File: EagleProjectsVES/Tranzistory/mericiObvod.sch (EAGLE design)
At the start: 100 parts, among them IC1 TLC272D, IC2 TLC272D, IC3 NE555D, IC4 NE555D, IC5 TLC271D, K1 M3XXH, K2 M3XXH, K3 M3XXH, K4 M3XXH, T3 BC557B, U12V SMKDSP_1,5/2

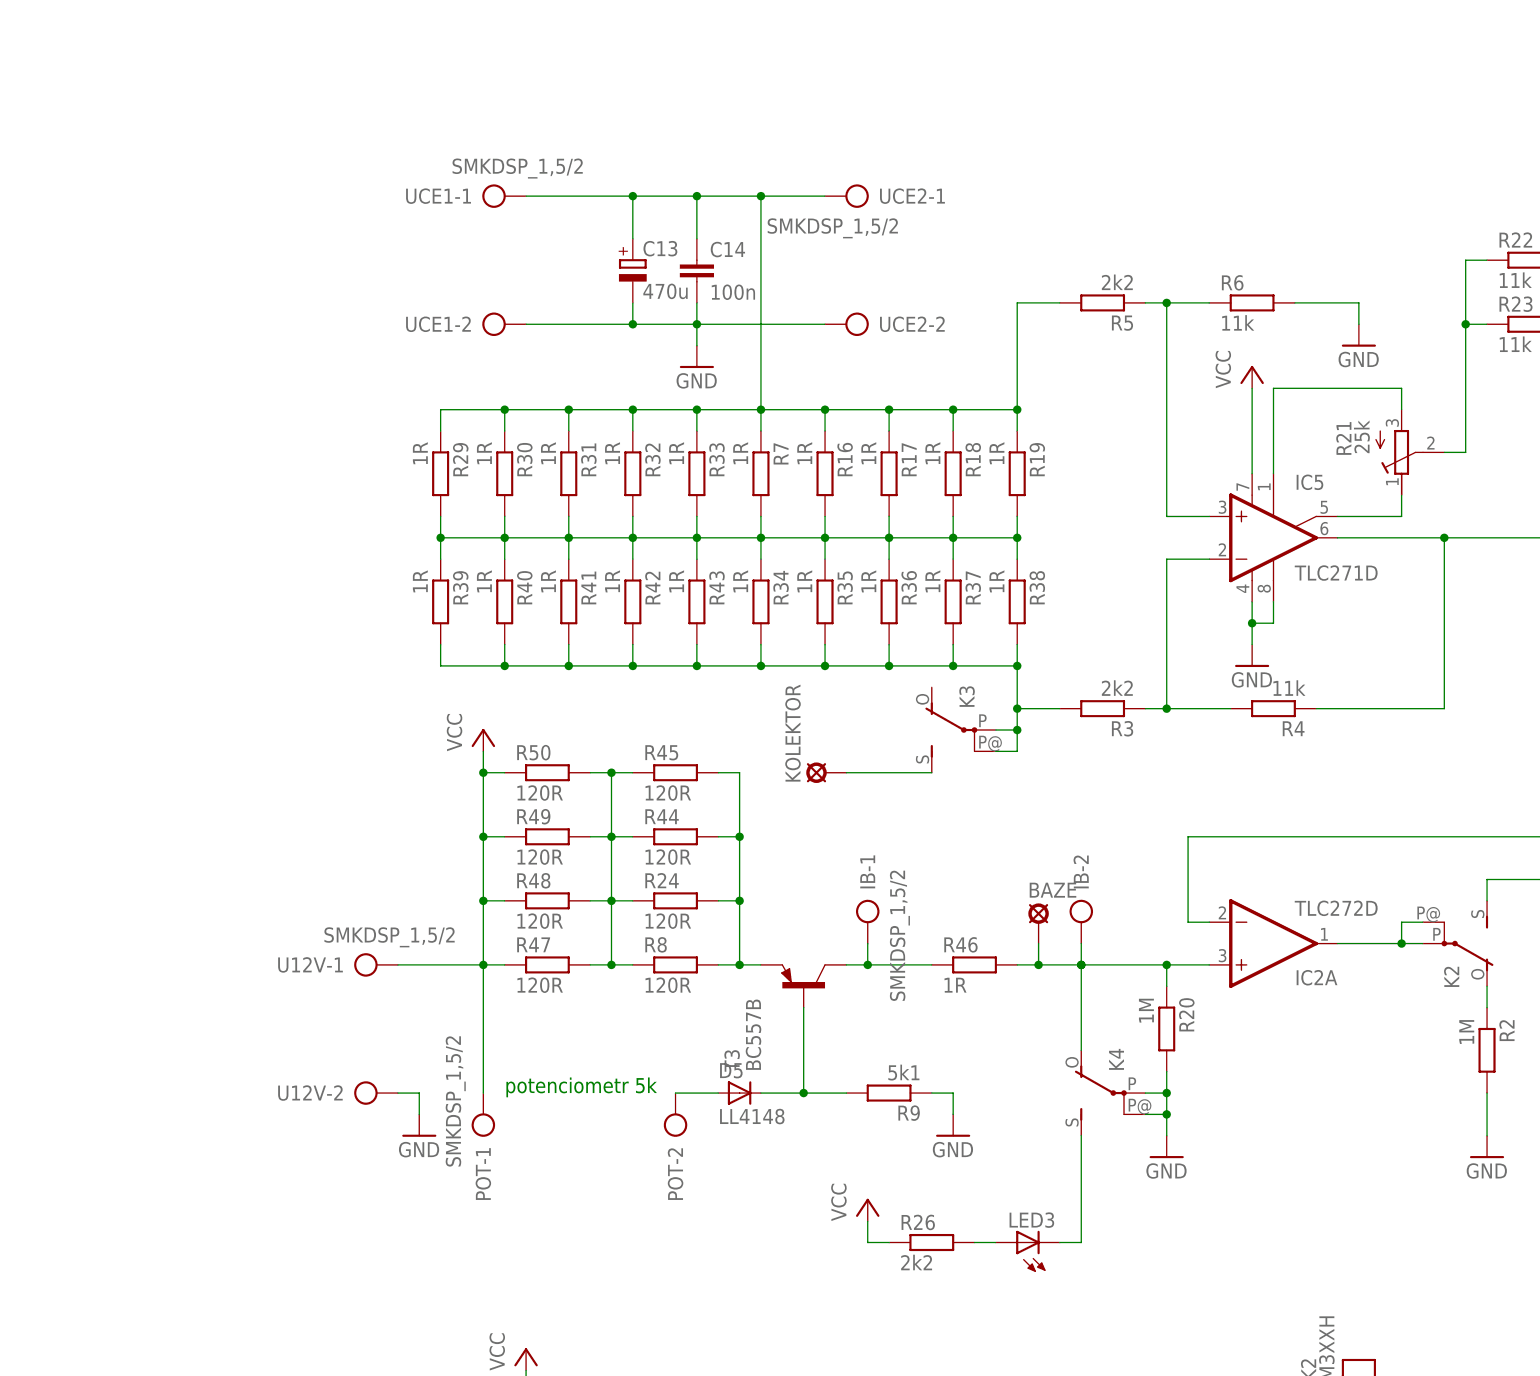
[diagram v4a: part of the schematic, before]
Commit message: DPS Tranzistory: - opraveny chyby v desce, nyni by mela byt pouzitelna az do 30 V UCE
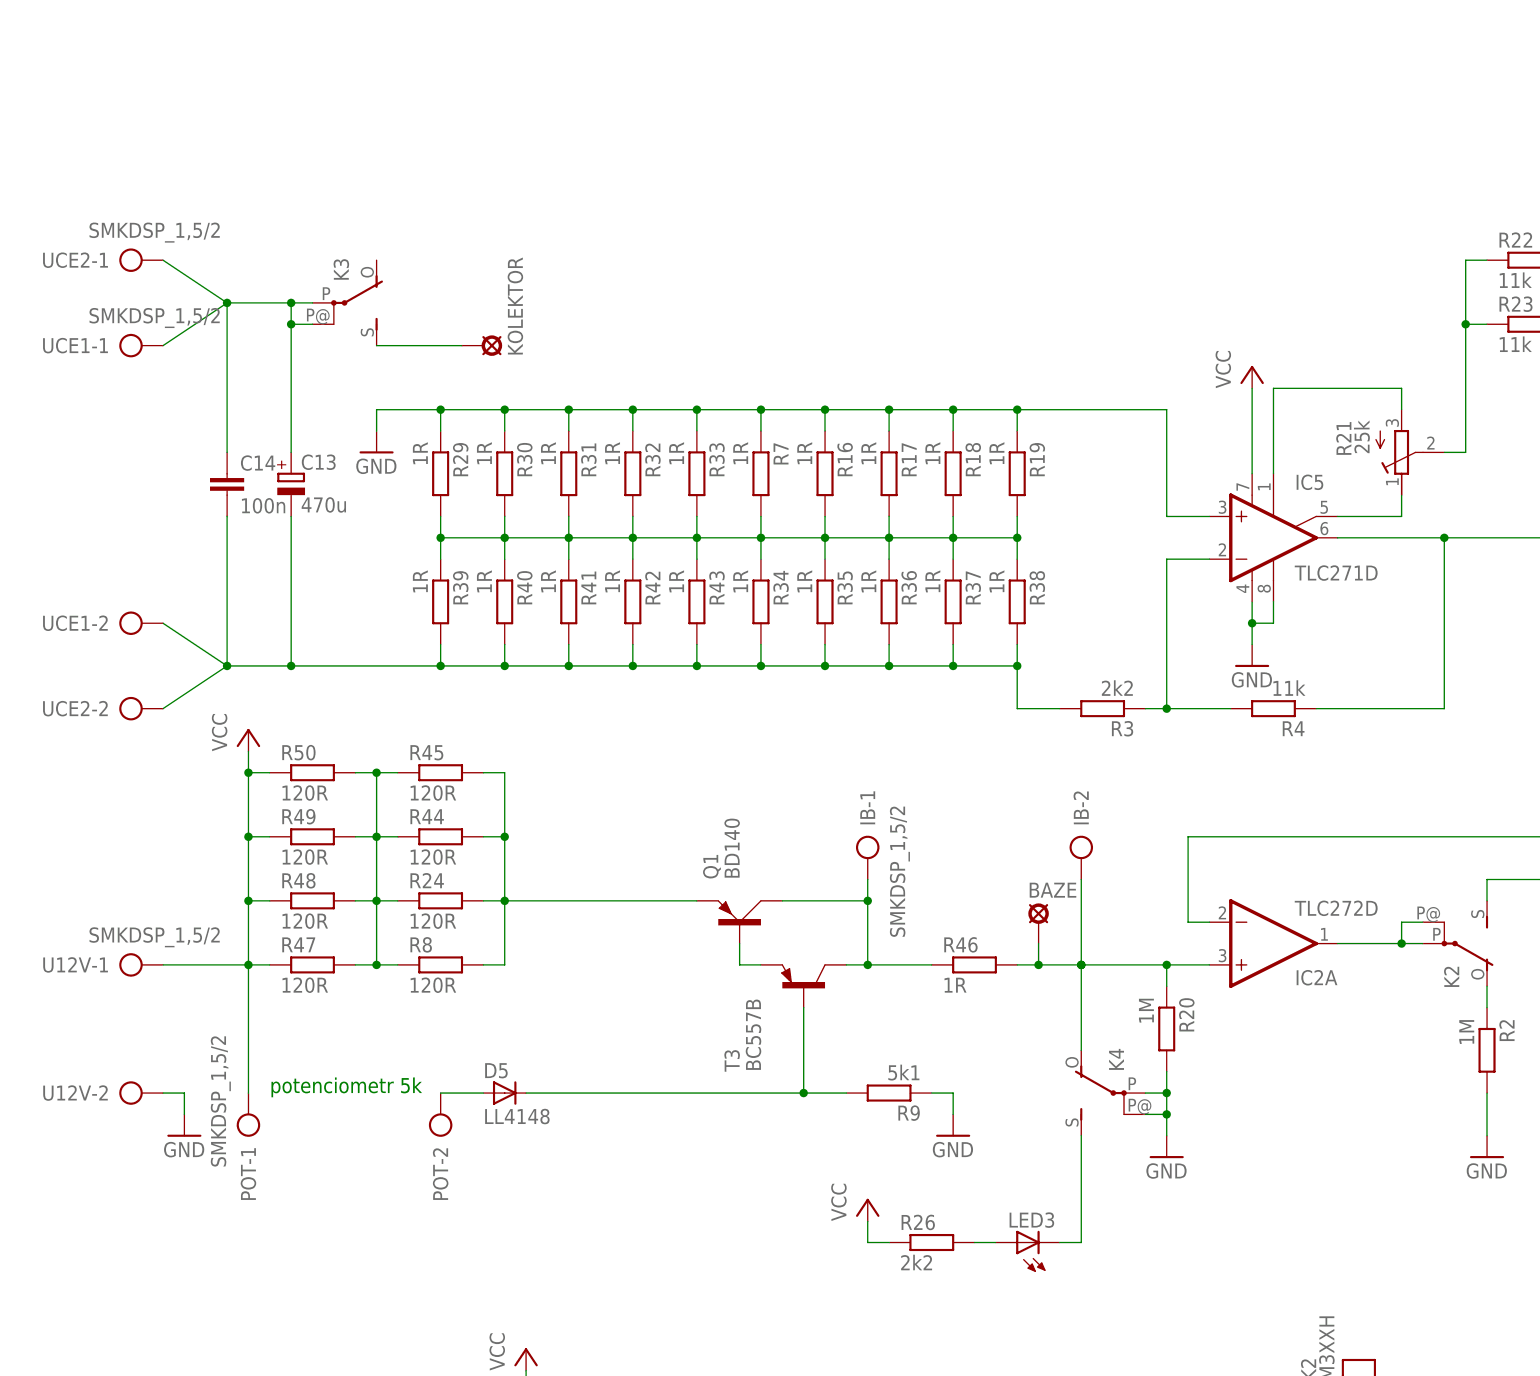
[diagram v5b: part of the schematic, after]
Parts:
- removed R5: 2k2, rcl:R-EU_R0805
- removed R6: 11k, rcl:R-EU_R0805
- added Q1: BD140, transistor-power:BD140
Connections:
- removed net N$11: C13.+, C14.1, R16.1, R17.1, R18.1, R19.1, R29.1, R30.1, R31.1, R32.1, R33.1, R5.2, R7.1, UCE1-1.KL, UCE2-1.KL
- new net N$40: C13.+, C14.1, K32.P, K32.P@1, UCE1-1.KL, UCE2-1.KL
- net GND: now also IC5.+IN, R16.1, R17.1, R18.1, R19.1, R29.1, R30.1, R31.1, R32.1, R33.1, R7.1; no longer C13.-, C14.2, R6.2, UCE1-2.KL, UCE2-2.KL
- net N$16: now also Q1.C
- net N$17: now also Q1.E; no longer T3.E
- net N$48: now also C13.-, C14.2, UCE1-2.KL, UCE2-2.KL; no longer K32.P, K32.P@1
- net N$9: now also Q1.B, T3.E; no longer IC5.+IN, R5.1, R6.1
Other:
- moved on the sheet: C13, C14, D5, IB-1, IB-2, K3, KOLEKTOR, POT-1, POT-2, R24, R44, R45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

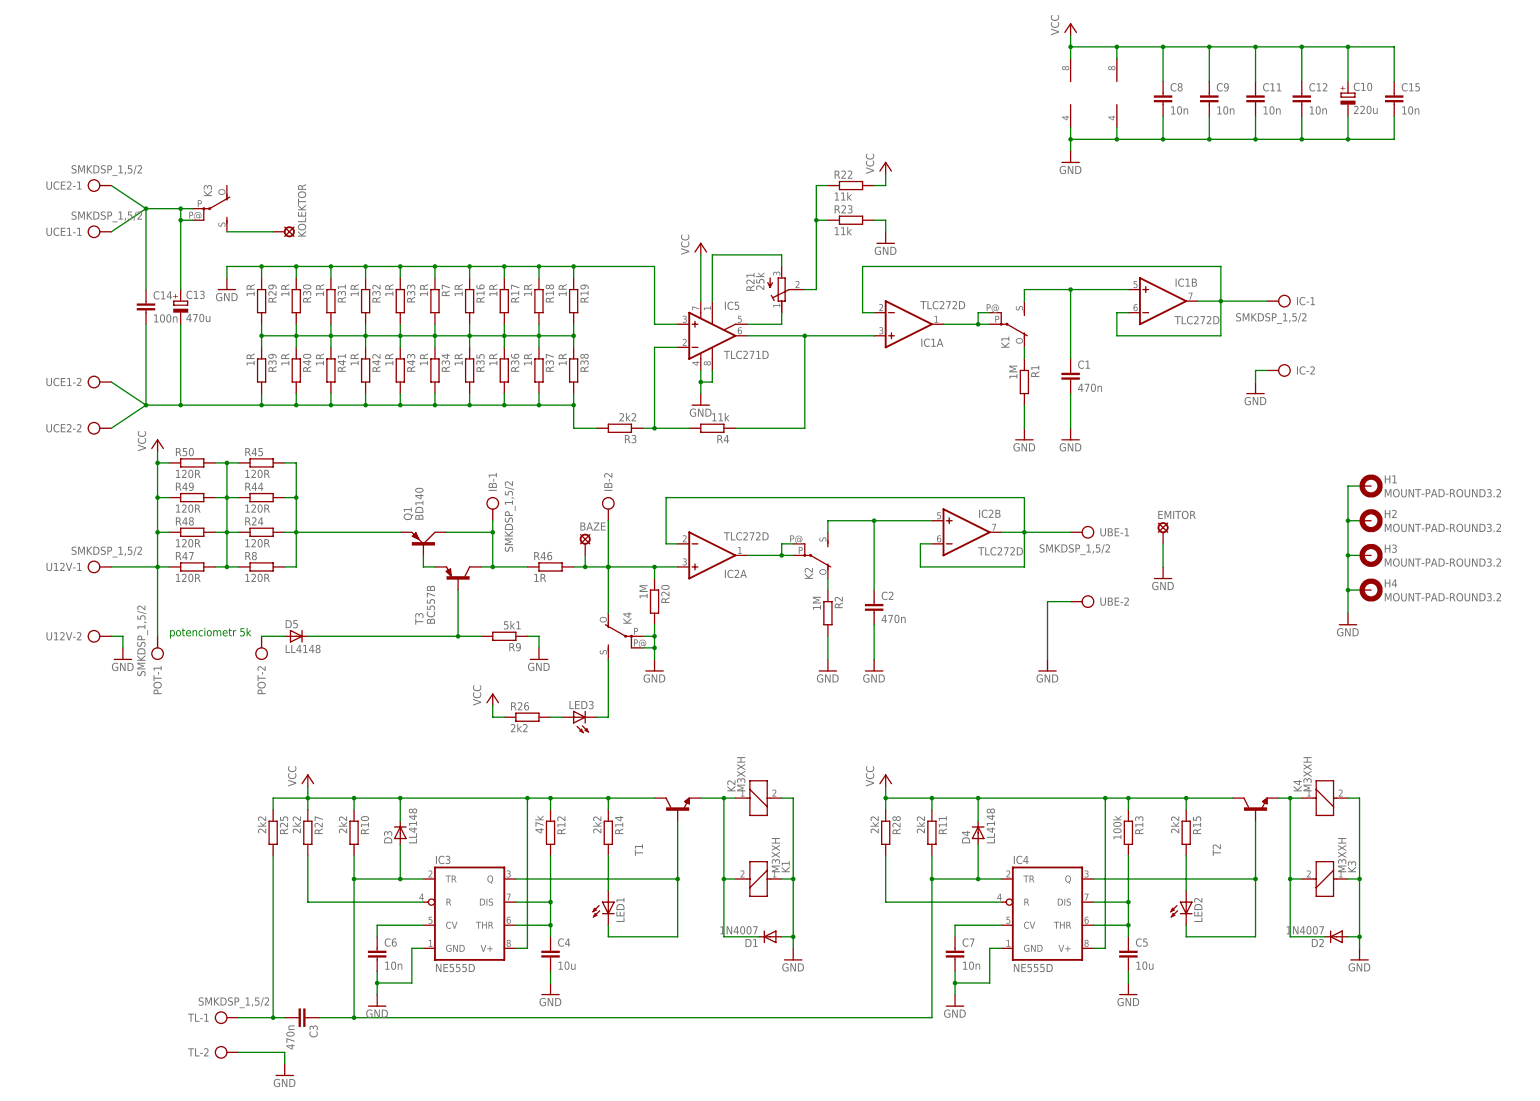
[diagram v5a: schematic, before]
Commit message: DPS Tranzisotry: - snizeno zesileni zpetne vazby - pridan odpor ke kondenzatoru sample-hold tak, aby vytvoril integracni clanek.
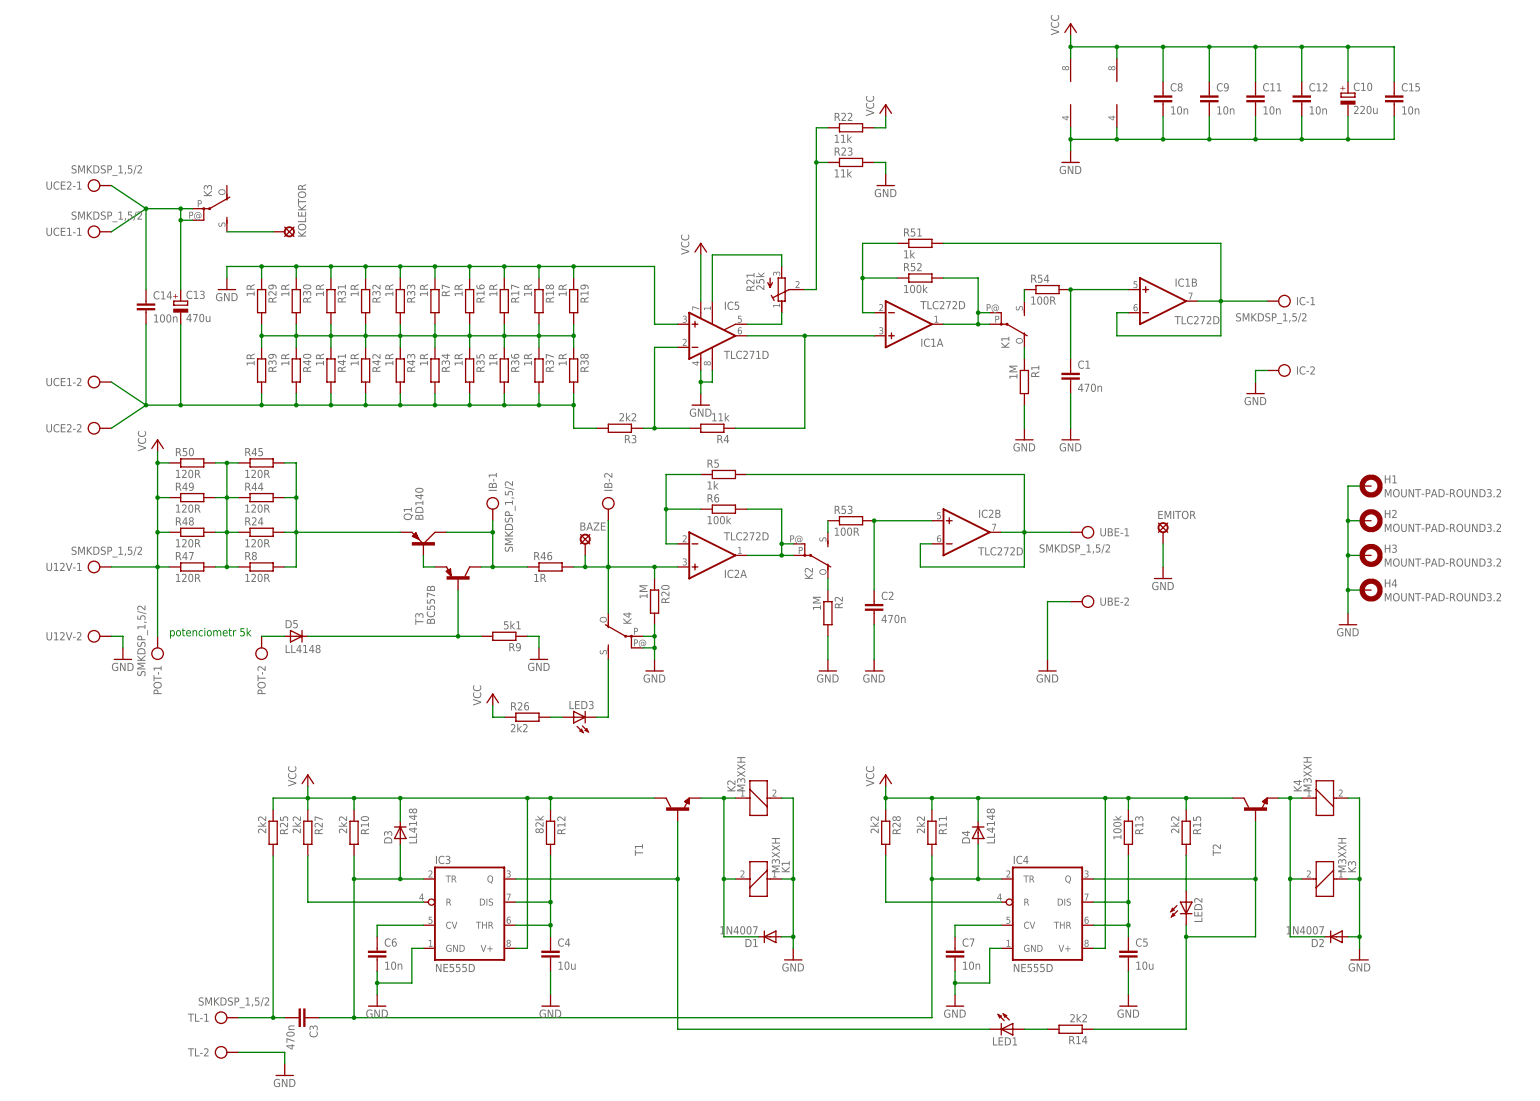
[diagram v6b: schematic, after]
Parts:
- added R5, R51: 1k, rcl:R-EU_R0805
- added R52, R6: 100k, rcl:R-EU_R0805
- added R53, R54: 100R, rcl:R-EU_R0805
- R12: value 47k -> 82k
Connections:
- new net N$11: IC2A.-IN, R5.1, R6.1
- new net N$39: IC1A.-IN, R51.1, R52.1
- new net N$41: K12.S, R54.1
- new net N$42: K22.S, R53.1
- net N$10: now also R51.2; no longer IC1A.-IN
- net N$2: now also R5.2; no longer IC2A.-IN
- net N$20: now also R14.1
- net N$3: now also R54.2; no longer K12.S
- net N$4: now also R53.2; no longer K22.S
- net N$5: now also R6.2
- net N$6: now also R52.2
- net VCC: no longer R14.1
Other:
- moved on the sheet: LED1, R14, R22, R23

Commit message: Eagle: - vybijec pro Papeze - tranzistory pred odeslanim do pragoboardu - navrh zdroju proudu
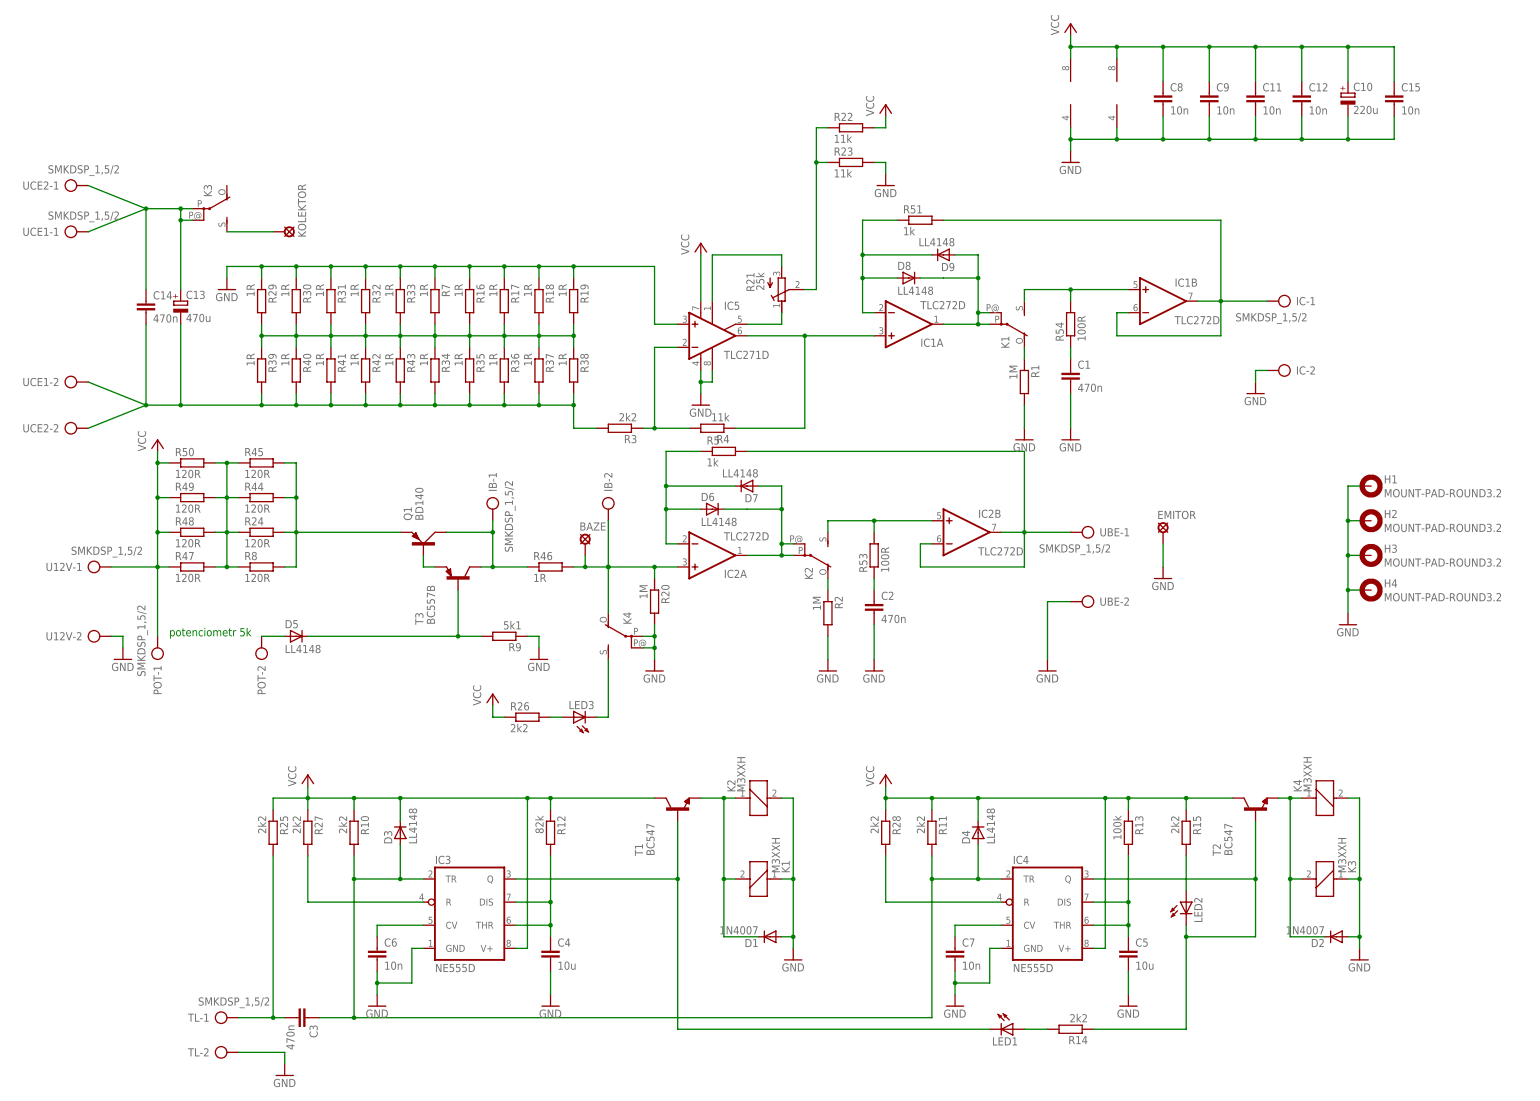
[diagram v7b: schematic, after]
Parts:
- removed R52, R6: 100k, rcl:R-EU_R0805
- added D6, D7, D8, D9: LL4148, semicon-smd-ipc:D-SOD-80
- C14: value 100n -> 470n
- T1, T2: value (none) -> BC547
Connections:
- net N$11: now also D6.A, D7.C; no longer R6.1
- net N$3: now also R54.1; no longer IC1B.+IN, R54.2
- net N$39: now also D8.A, D9.C; no longer R52.1
- net N$4: now also R53.1; no longer IC2B.+IN, R53.2
- net N$41: now also IC1B.+IN, R54.2; no longer R54.1
- net N$42: now also IC2B.+IN, R53.2; no longer R53.1
- net N$5: now also D6.C, D7.A; no longer R6.2
- net N$6: now also D8.C, D9.A; no longer R52.2
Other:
- moved on the sheet: R5, R51, R53, R54, UCE1-1, UCE1-2, UCE2-1, UCE2-2
